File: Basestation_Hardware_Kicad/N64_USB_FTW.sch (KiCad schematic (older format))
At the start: 28 parts, among them IC1 ATMEGA8-AI, P1 CONN_3X2, P2 CONN_5X2, U1 LM317, X1 12mhz, X2 USB-MB-S

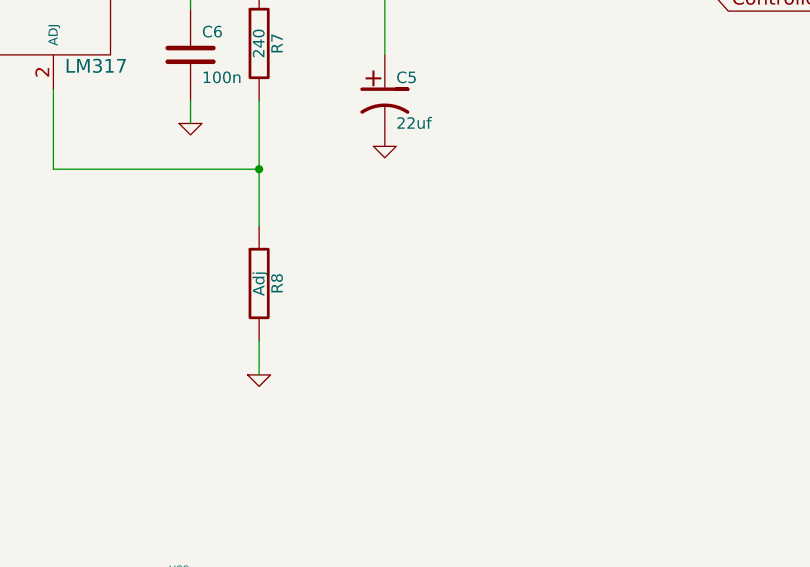
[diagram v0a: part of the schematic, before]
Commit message: continued Part sourcing - added some missing values to both designs
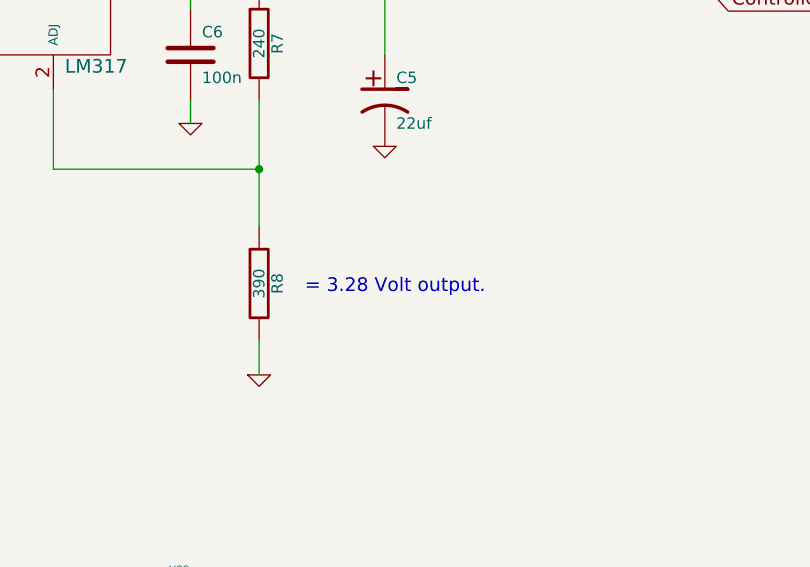
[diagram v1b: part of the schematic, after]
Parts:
- R8: value Adj -> 390
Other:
- note added: "= 3.28 Volt output."
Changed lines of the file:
@@
-EESchema Schematic File Version 2  date 09-05-2012 21:22:02
+EESchema Schematic File Version 2  date 04-06-2012 18:07:27
 LIBS:power
 LIBS:device
@@
 Sheet 1 1
 Title ""
-Date "9 may 2012"
+Date "4 jun 2012"
 Rev ""
 Comp ""
@@
 Comment4 ""
 $EndDescr
+Text Notes 12500 3700 0    60   ~ 0
+= 3.28 Volt output.
 Wire Wire Line
 	7800 4600 7700 4600
@@
 P 12300 3650
 F 0 "R8" V 12380 3650 50  0000 C CNN
-F 1 "Adj" V 12300 3650 50  0000 C CNN
+F 1 "390" V 12300 3650 50  0000 C CNN
 	1    12300 3650
 	1    0    0    -1

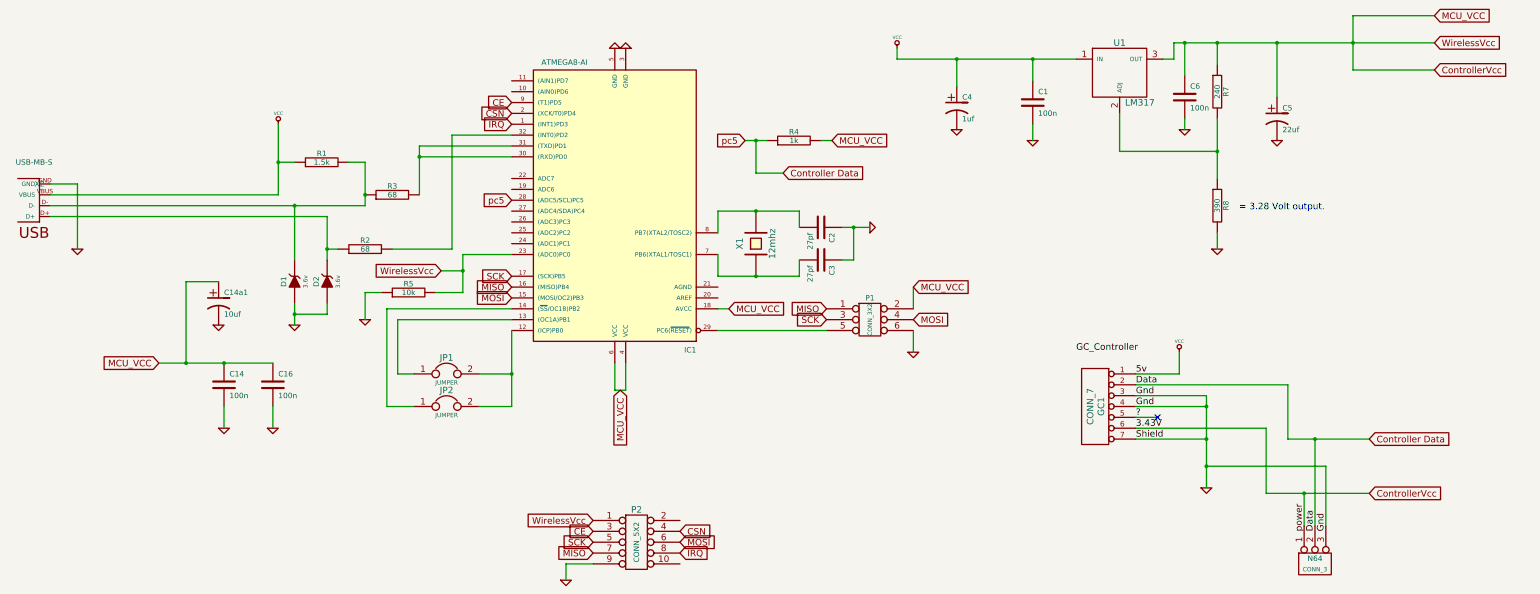
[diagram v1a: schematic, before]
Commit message: cleaned the layout, changed LM317 Vout to 3.35V, had cake
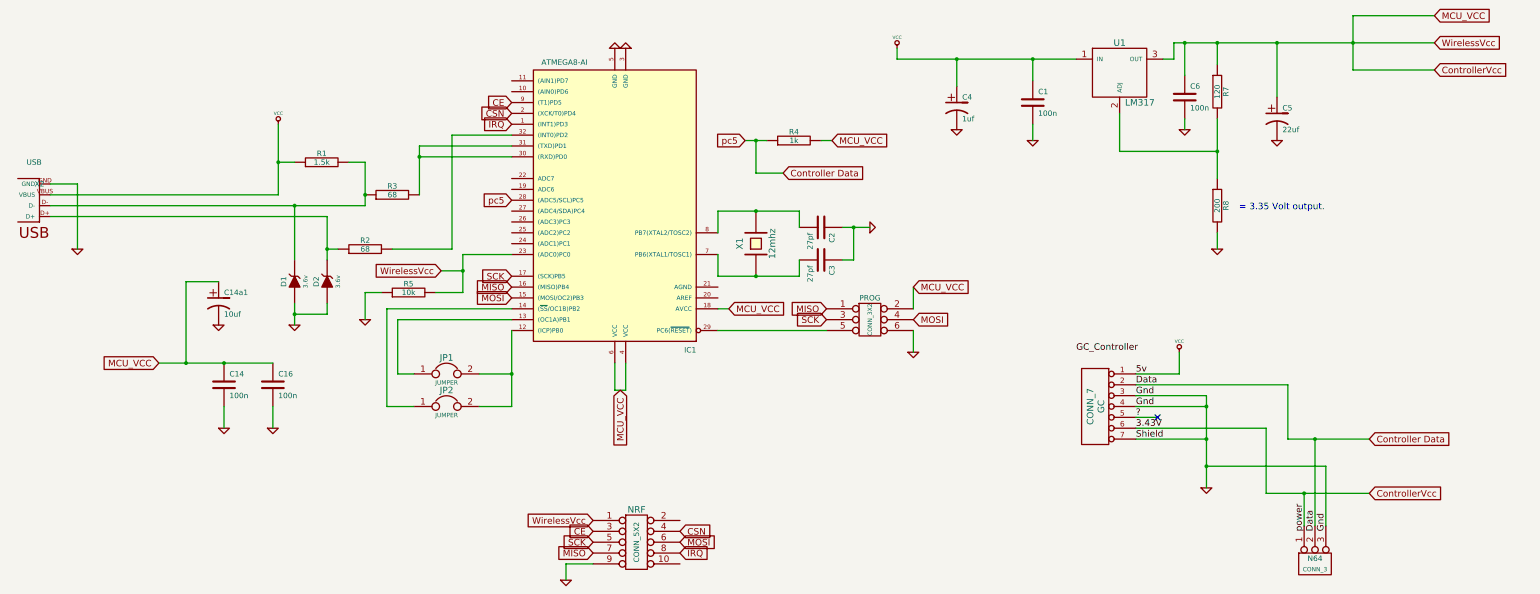
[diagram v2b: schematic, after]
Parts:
- R7: value 240 -> 120
- R8: value 390 -> 200
- X2: value USB-MB-S -> USB
- renumbered GC1 to GC, P2 to NRF, P1 to PROG
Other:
- note added: "= 3.35 Volt output."
- note removed: "= 3.28 Volt output."
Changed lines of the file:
@@
-EESchema Schematic File Version 2  date 04-06-2012 18:07:27
+EESchema Schematic File Version 2  date 09-06-2012 11:32:36
 LIBS:power
 LIBS:device
@@
 Sheet 1 1
 Title ""
-Date "4 jun 2012"
+Date "9 jun 2012"
 Rev ""
 Comp ""
@@
 $EndDescr
 Text Notes 12500 3700 0    60   ~ 0
-= 3.28 Volt output.
+= 3.35 Volt output.
 Wire Wire Line
 	7800 4600 7700 4600
@@
 MCU_VCC
 $Comp
-L CONN_5X2 P2
+L CONN_5X2 NRF
 U 1 1 4F68E2A7
 P 6950 6750
-F 0 "P2" H 6950 7050 60  0000 C CNN
+F 0 "NRF" H 6950 7050 60  0000 C CNN
 F 1 "CONN_5X2" V 6950 6750 50  0000 C CNN
 	1    6950 6750
@@
 P 1450 3450
 F 0 "X2" H 1450 3450 50  0000 C CNN
-F 1 "USB-MB-S" H 1500 3250 50  0000 C CNN
+F 1 "USB" H 1500 3250 50  0000 C CNN
 F 2 "con-usb-USB-MB-S" H 1450 3350 50  0001 C CNN
 	1    1450 3450
@@
 GC_Controller
 $Comp
-L CONN_7 GC1
+L CONN_7 GC
 U 1 1 4F452C08
 P 11200 5500
-F 0 "GC1" V 11170 5500 60  0000 C CNN
+F 0 "GC" V 11170 5500 60  0000 C CNN
 F 1 "CONN_7" V 11270 5500 60  0000 C CNN
 	1    11200 5500
@@
 P 12300 2600
 F 0 "R7" V 12380 2600 50  0000 C CNN
-F 1 "240" V 12300 2600 50  0000 C CNN
+F 1 "120" V 12300 2600 50  0000 C CNN
 	1    12300 2600
 	1    0    0    -1
@@
 P 12300 3650
 F 0 "R8" V 12380 3650 50  0000 C CNN
-F 1 "390" V 12300 3650 50  0000 C CNN
+F 1 "200" V 12300 3650 50  0000 C CNN
 	1    12300 3650
 	1    0    0    -1
@@
 pc5
 $Comp
-L GND #PWR016
+L GND #PWR015
 U 1 1 4F43FD84
 P 6750 2200
-F 0 "#PWR016" H 6750 2200 30  0001 C CNN
+F 0 "#PWR015" H 6750 2200 30  0001 C CNN
 F 1 "GND" H 6750 2130 30  0001 C CNN
 	1    6750 2200
@@
 $EndComp
 $Comp
-L GND #PWR017
+L GND #PWR016
 U 1 1 4F43FD6B
 P 6850 2200
-F 0 "#PWR017" H 6850 2200 30  0001 C CNN
+F 0 "#PWR016" H 6850 2200 30  0001 C CNN
 F 1 "GND" H 6850 2130 30  0001 C CNN
 	1    6850 2200
@@
 $EndComp
 $Comp
-L GND #PWR018
+L GND #PWR017
 U 1 1 4F43FC5C
 P 9500 5000
-F 0 "#PWR018" H 9500 5000 30  0001 C CNN
+F 0 "#PWR017" H 9500 5000 30  0001 C CNN
 F 1 "GND" H 9500 4930 30  0001 C CNN
 	1    9500 5000
@@
 SCK
 $Comp
-L GND #PWR019
+L GND #PWR018
 U 1 1 4F43F2E9
 P 3100 4750
-F 0 "#PWR019" H 3100 4750 30  0001 C CNN
+F 0 "#PWR018" H 3100 4750 30  0001 C CNN
 F 1 "GND" H 3100 4680 30  0001 C CNN
 	1    3100 4750
@@
 $EndComp
 $Comp
-L GND #PWR020
+L GND #PWR019
 U 1 1 4F43EE47
 P 3800 4750
-F 0 "#PWR020" H 3800 4750 30  0001 C CNN
+F 0 "#PWR019" H 3800 4750 30  0001 C CNN
 F 1 "GND" H 3800 4680 30  0001 C CNN
 	1    3800 4750
@@
 $EndComp
 $Comp
-L CONN_3X2 P1
+L CONN_3X2 PROG
 U 1 1 4F43E0D8
 P 9100 4750
-F 0 "P1" H 9100 5000 50  0000 C CNN
+F 0 "PROG" H 9100 5000 50  0000 C CNN
 F 1 "CONN_3X2" V 9100 4800 40  0000 C CNN
 	1    9100 4750
@@
 $EndComp
 $Comp
-L VCC #PWR021
+L VCC #PWR020
 U 1 1 4F43DEFD
 P 3650 2900
-F 0 "#PWR021" H 3650 3000 30  0001 C CNN
+F 0 "#PWR020" H 3650 3000 30  0001 C CNN
 F 1 "VCC" H 3650 3000 30  0000 C CNN
 	1    3650 2900
